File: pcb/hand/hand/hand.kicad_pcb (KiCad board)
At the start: 2 copper layers, 175.1 x 138.9 mm, 41 parts, among them J1 Conn_01x15

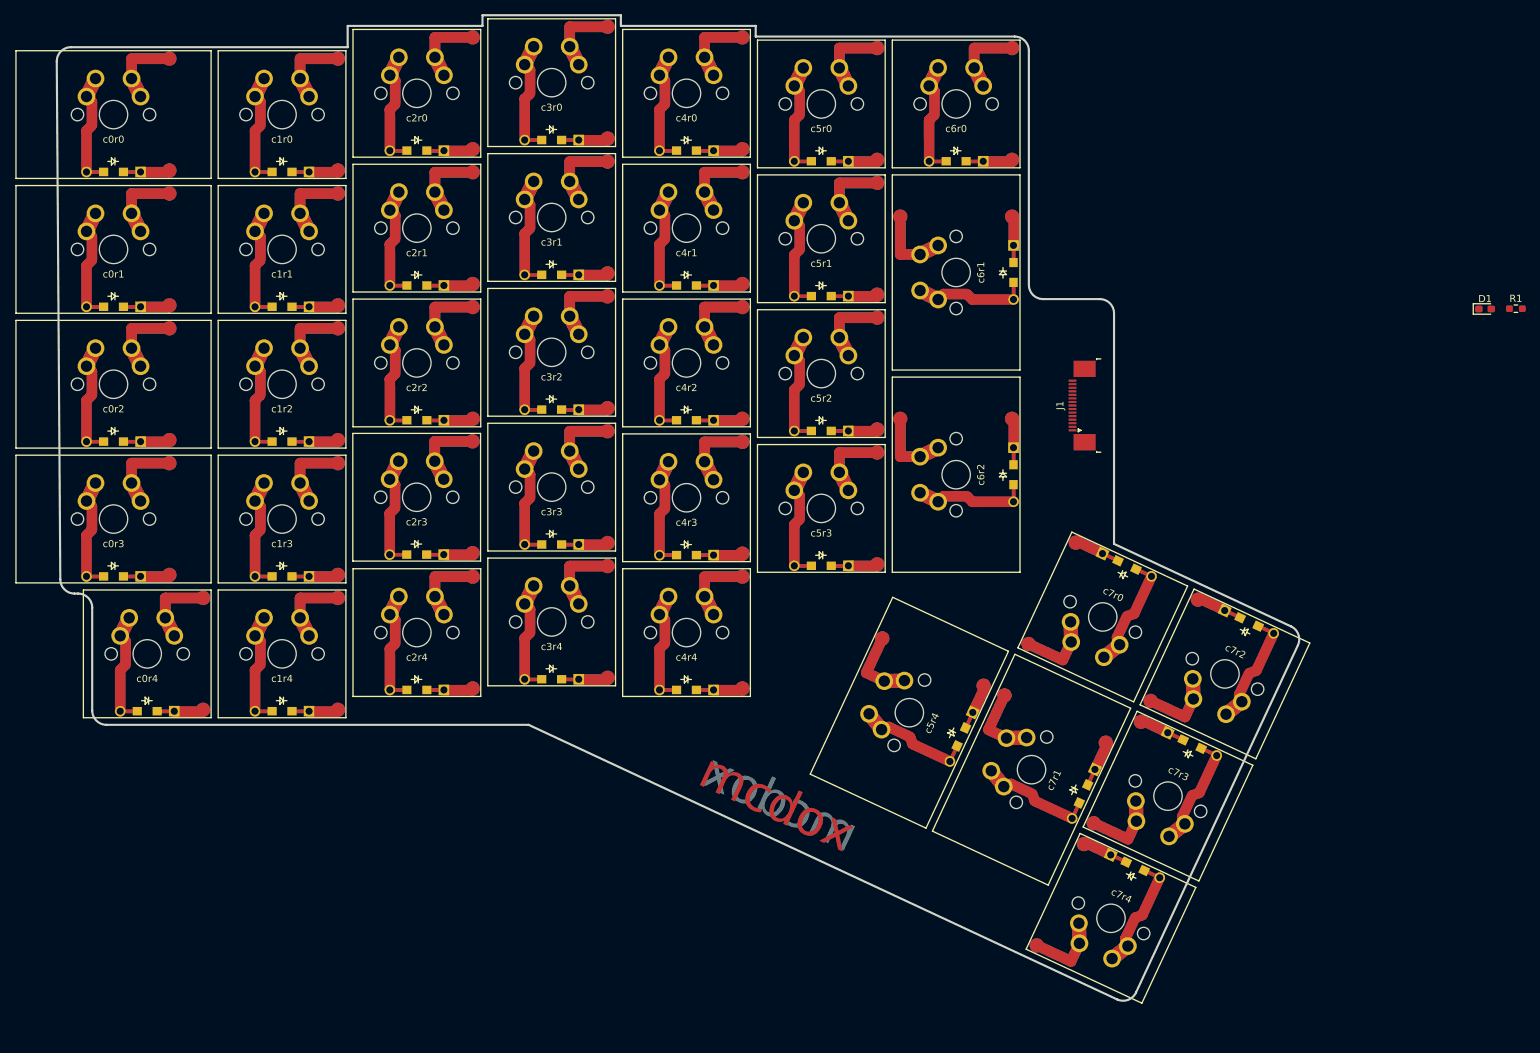
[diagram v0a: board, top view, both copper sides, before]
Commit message: pcb/hand Move testpoint pads for easier routing.
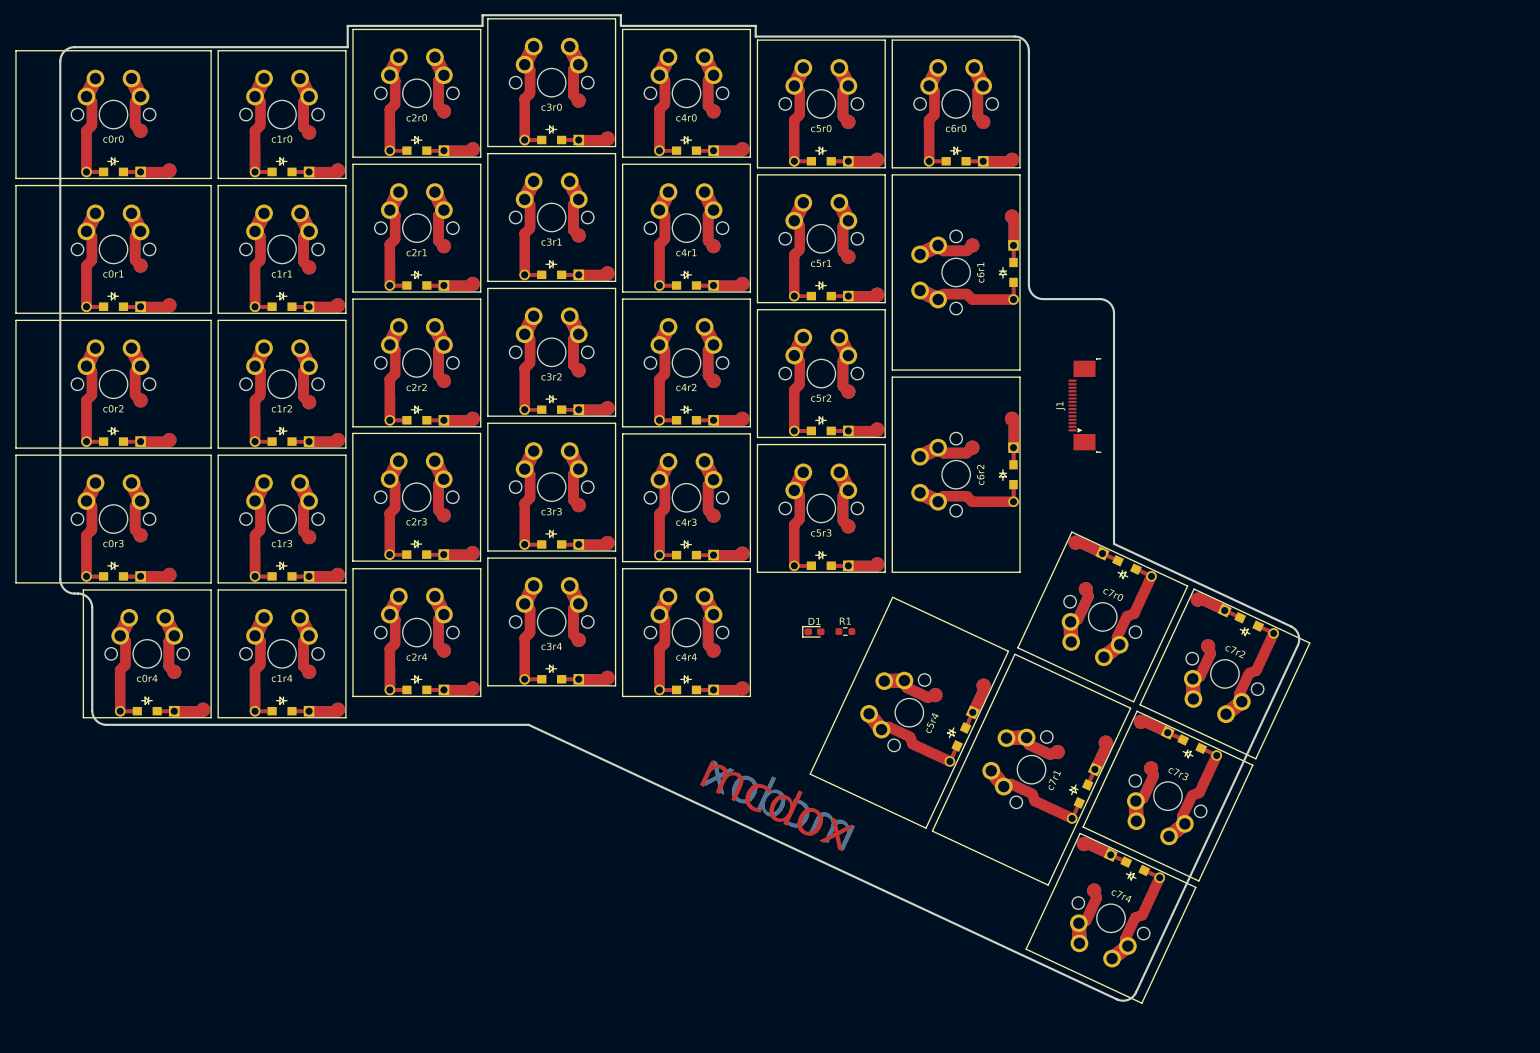
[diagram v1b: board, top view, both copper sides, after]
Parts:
- moved D1 104.9 mm to (142.8, 111.9)
- moved R1 104.9 mm to (147.1, 111.9)
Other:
- board size 175.1 x 138.9 mm -> 174.6 x 138.9 mm

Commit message: pcb/hand Partial workaround for issue with copper graphics in footprint. WIP
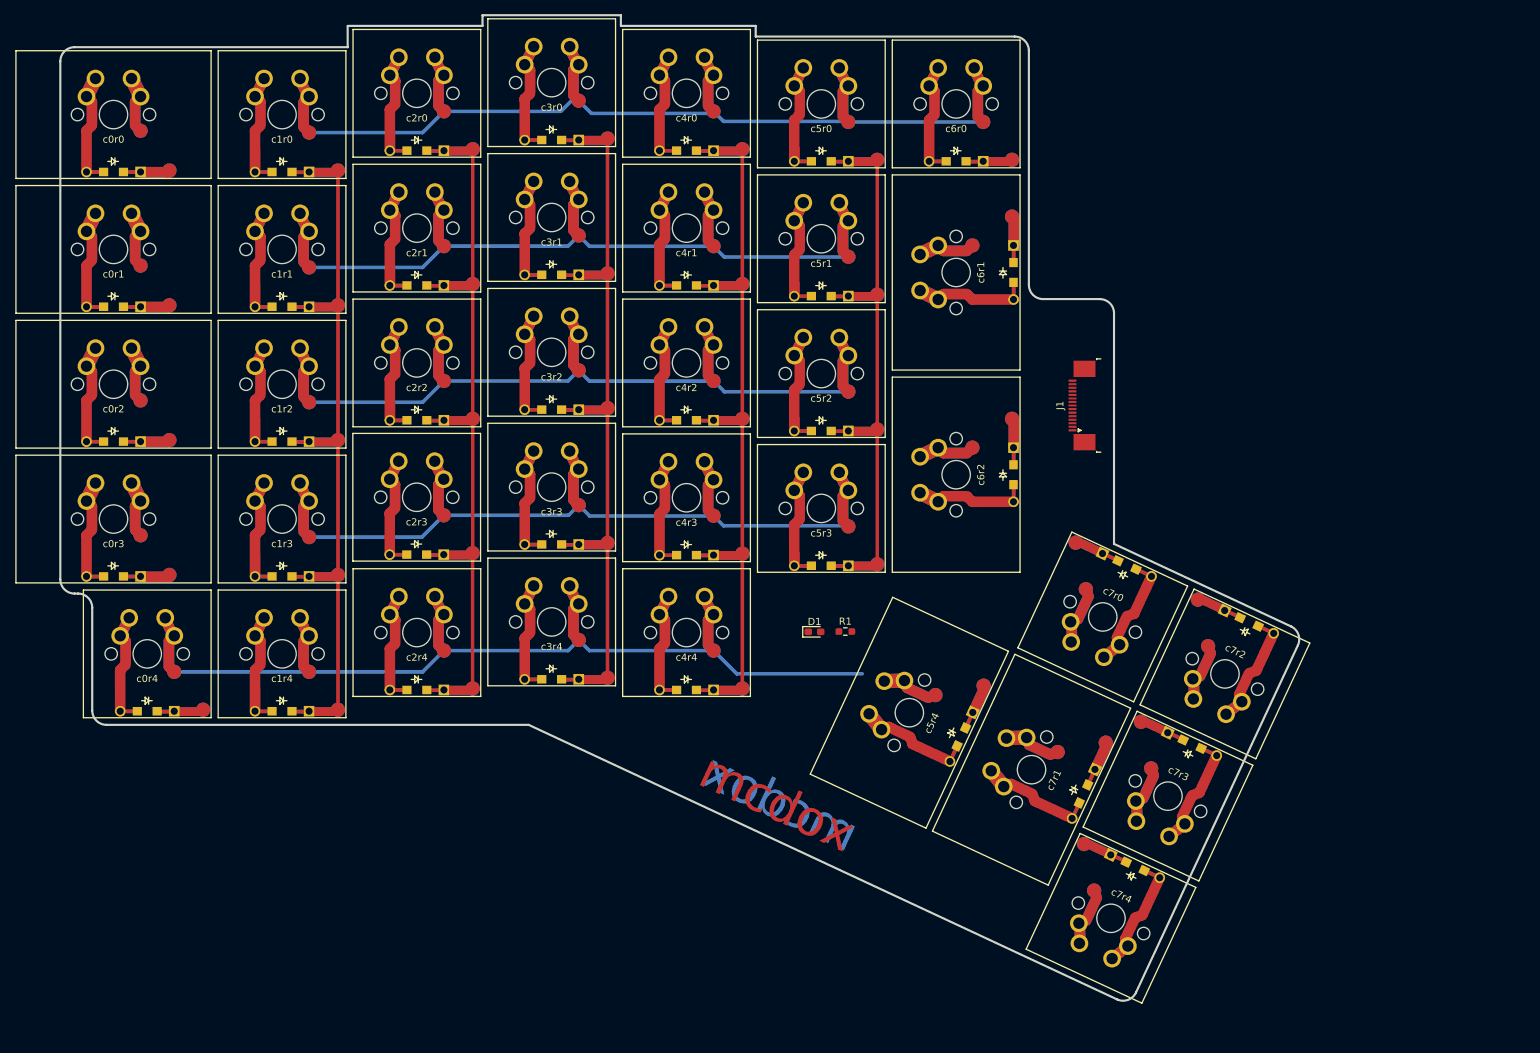
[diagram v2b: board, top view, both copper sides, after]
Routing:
- net row4: track 0.00 -> 100.8 mm
- net row0: track 0.00 -> 98.8 mm
- net row3: track 0.00 -> 79.8 mm
- net row1: track 0.00 -> 79.1 mm
- net row2: track 0.00 -> 79.1 mm
- net col2: track 0.00 -> 76.0 mm
- net col4: track 0.00 -> 76.0 mm
- net col3: track 0.00 -> 76.0 mm
- net col1: track 0.00 -> 76.0 mm
- net col5: track 0.00 -> 57.0 mm

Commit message: pcb/hand 0603 diode and pad-hack on 1.5x footprints.
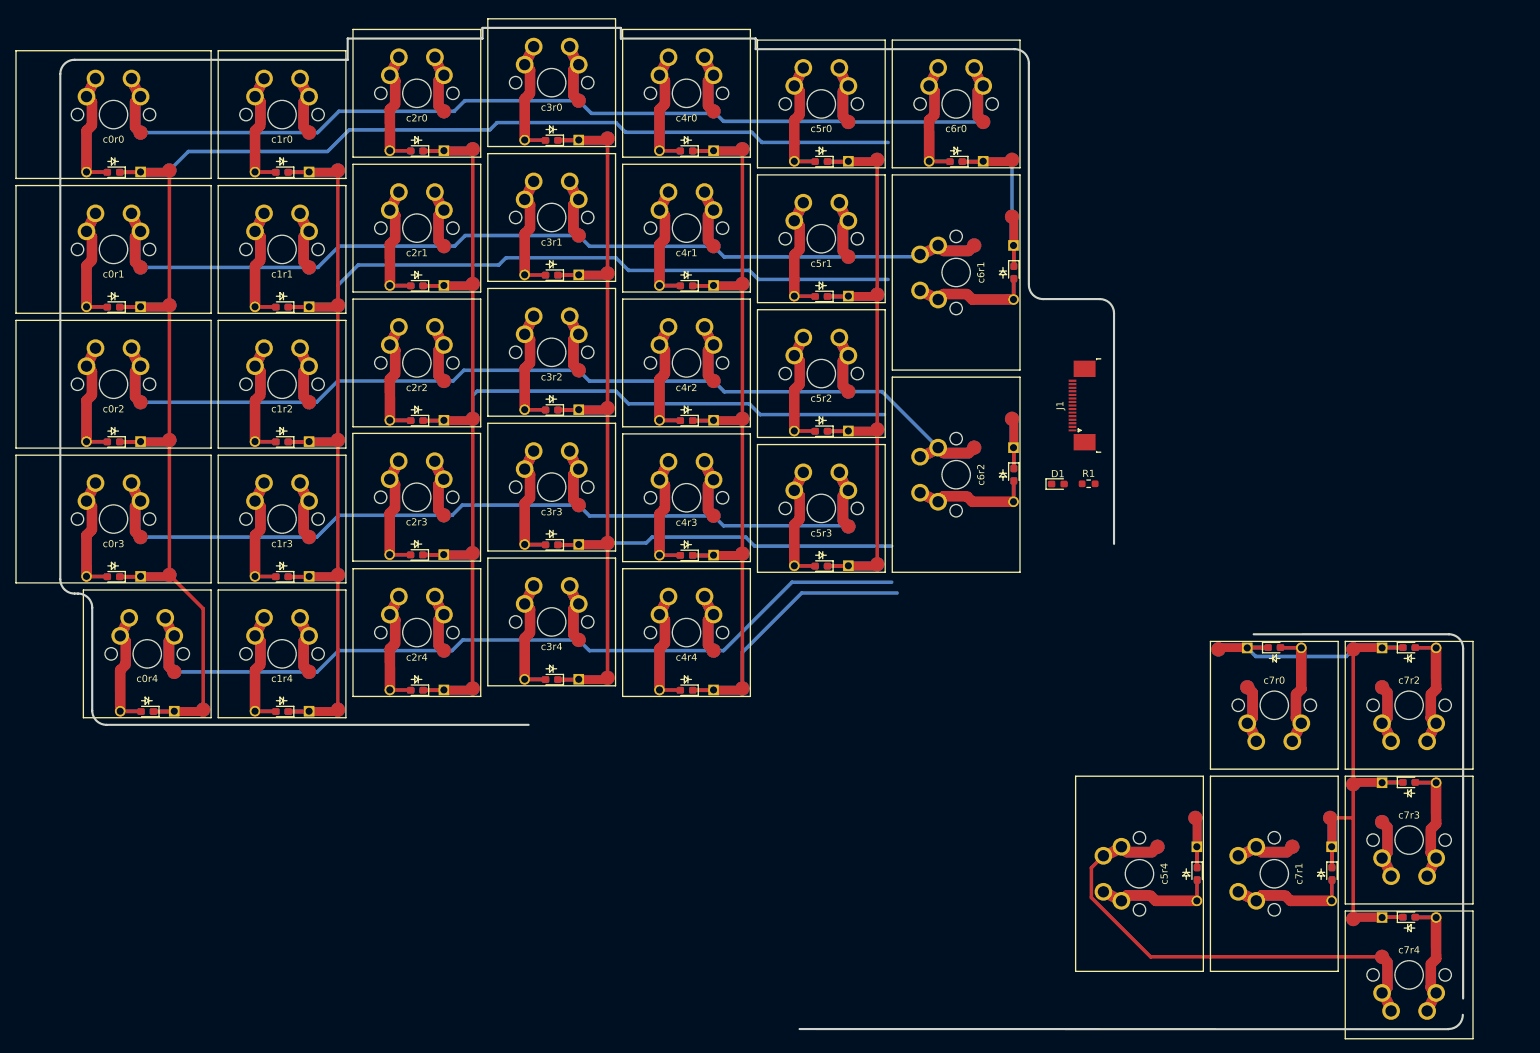
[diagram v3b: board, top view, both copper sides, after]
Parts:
- moved c7r4 42.8 mm to (226.6, 160.2), turned to 180 degrees
- moved D1 40.1 mm to (177.1, 91.1)
- moved R1 40.1 mm to (181.4, 91.0)
- moved c5r4 39.6 mm to (188.6, 146.0), turned to 90 degrees
- moved c7r1 37.2 mm to (207.6, 146.0), turned to 90 degrees
- moved c7r3 34.5 mm to (226.6, 141.2), turned to 180 degrees
- moved c7r0 27.2 mm to (207.6, 122.2), turned to 180 degrees
- moved c7r2 26.3 mm to (226.6, 122.2), turned to 180 degrees
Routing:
- net col0: track 0.00 -> 254.2 mm
- net col1: track 76.0 -> 230.3 mm
- net col2: track 76.0 -> 210.0 mm
- net col7: track 0.00 -> 128.2 mm
- net col3: track 76.0 -> 188.0 mm
- net col4: track 76.0 -> 177.4 mm
- net row4: track 100.8 -> 177.0 mm
- net col5: track 57.0 -> 128.0 mm
- net row2: track 79.1 -> 143.3 mm
- net row1: track 79.1 -> 137.7 mm
- net col6: track 0.00 -> 50.6 mm
- net row0: track 98.8 -> 147.3 mm
- net row3: track 79.8 -> 125.1 mm
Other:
- board size 174.6 x 138.9 mm -> 197.7 x 141.1 mm
- board text removed: "mcdox"

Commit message: hand/pcb Routing complete and proper NPTH holes without mask.
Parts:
- added J1: Conn_01x15, Connector_FFC-FPC:TE_1-84953-5_1x15-1MP_P1.0mm_Horizontal, F.Cu at (180.0, 78.0)
- added LED2: LED, Diode_SMD:D_0603_1608Metric_Pad1.05x0.95mm_HandSolder, B.Cu at (179.0, 93.4)
- added R2: 100, Resistor_SMD:R_0603_1608Metric_Pad0.98x0.95mm_HandSolder, B.Cu at (177.5, 93.4)
- J2: renamed from J1; footprint Connector_FFC-FPC:TE_1-1734839-5_1x15-1MP_P0.5mm_Horizontal -> Connector_FFC-FPC:TE_1-84953-5_1x15-1MP_P1.0mm_Horizontal; moved to B.Cu
- moved c7r4 44.1 mm to (183.2, 152.0), turned to 155 degrees
- moved c5r4 40.9 mm to (154.8, 123.0), turned to 65 degrees
- moved c7r1 38.6 mm to (172.0, 131.1), turned to 65 degrees
- moved c7r3 35.9 mm to (191.2, 134.8), turned to 245 degrees
- moved c7r0 28.5 mm to (182.0, 109.5), turned to 245 degrees
- moved c7r2 27.7 mm to (199.3, 117.6), turned to 245 degrees
- moved R1 4.64 mm to (177.5, 93.5), turned to 270 degrees
- moved LED1 3.10 mm to (179.0, 93.5), turned to 270 degrees
- moved J2 2.06 mm to (180.0, 78.0), turned to 270 degrees
- renumbered D1 to LED1
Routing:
- net row3: track 125.1 -> 267.9 mm, vias 0 -> 3
- net row0: track 147.3 -> 285.7 mm, vias 0 -> 2
- net row1: track 137.7 -> 275.9 mm, vias 0 -> 3
- net row2: track 143.3 -> 252.7 mm, vias 0 -> 2
- net row4: track 177.0 -> 242.2 mm, vias 0 -> 1
- net col0: track 254.2 -> 312.6 mm, vias 0 -> 2
- net col5: track 128.0 -> 184.5 mm, vias 0 -> 1
- net col6: track 50.6 -> 102.0 mm, vias 0 -> 1
- net col3: track 188.0 -> 226.5 mm, vias 0 -> 3
- net col1: track 230.3 -> 267.9 mm, vias 0 -> 2
- net col2: track 210.0 -> 244.5 mm, vias 0 -> 2
- net +3V3: track 0.00 -> 28.3 mm, vias 0 -> 1
- net col4: track 177.4 -> 205.6 mm, vias 0 -> 3
- net GND: track 0.00 -> 21.4 mm, vias 0 -> 1
- net col7: track 128.2 -> 145.9 mm, vias 0 -> 1
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- added copper zone on B.Cu, net (none)
- added copper zone on F.Cu, net (none)
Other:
- board size 197.7 x 141.1 mm -> 172.5 x 135.2 mm
- board text added: "mcdox"
